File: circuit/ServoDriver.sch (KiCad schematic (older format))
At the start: 0 parts

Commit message: 変更点忘れた
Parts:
- added C?: C, symbol C
- added J?: servo0, symbol CONN_01X03
- added J? (x2): servo2, symbol CONN_01X03
- added J?: servo1, symbol CONN_01X03
- added U?: STM32F042K6Tx, LQFP32, symbol STM32F042K6Tx
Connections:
- new net +3V3: C?.1, U?.1 (VDD), U?.17 (VDDIO2), U?.5 (VDDA)
- new net GND: C?.2, U?.16 (VSS), U?.32 (VSSA)

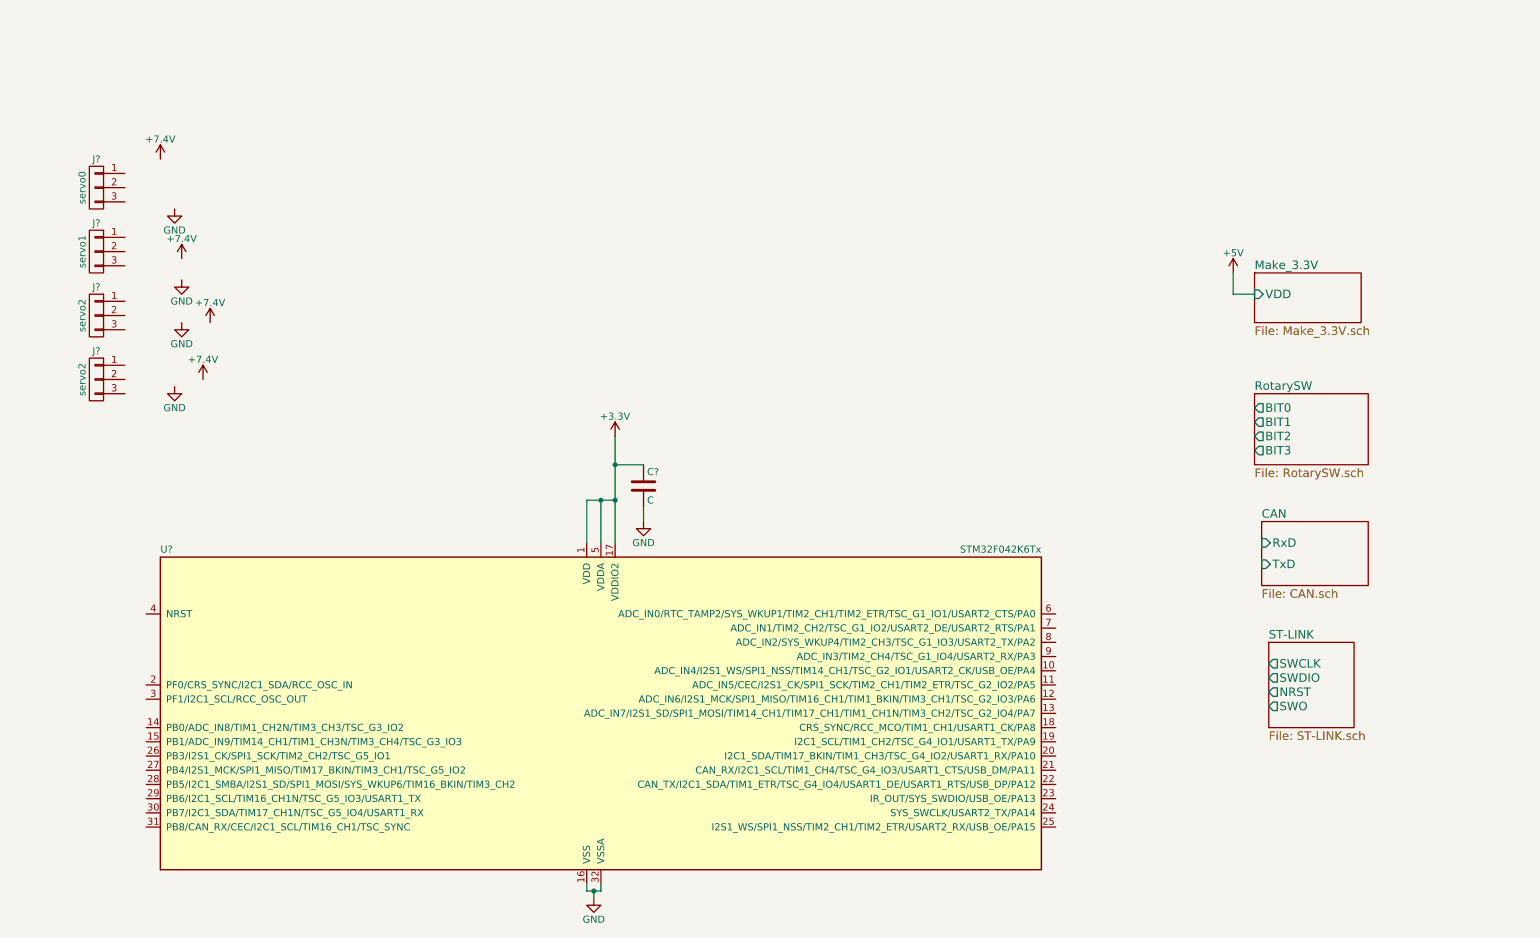
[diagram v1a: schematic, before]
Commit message: サーボの制御信号絶縁とシート分け
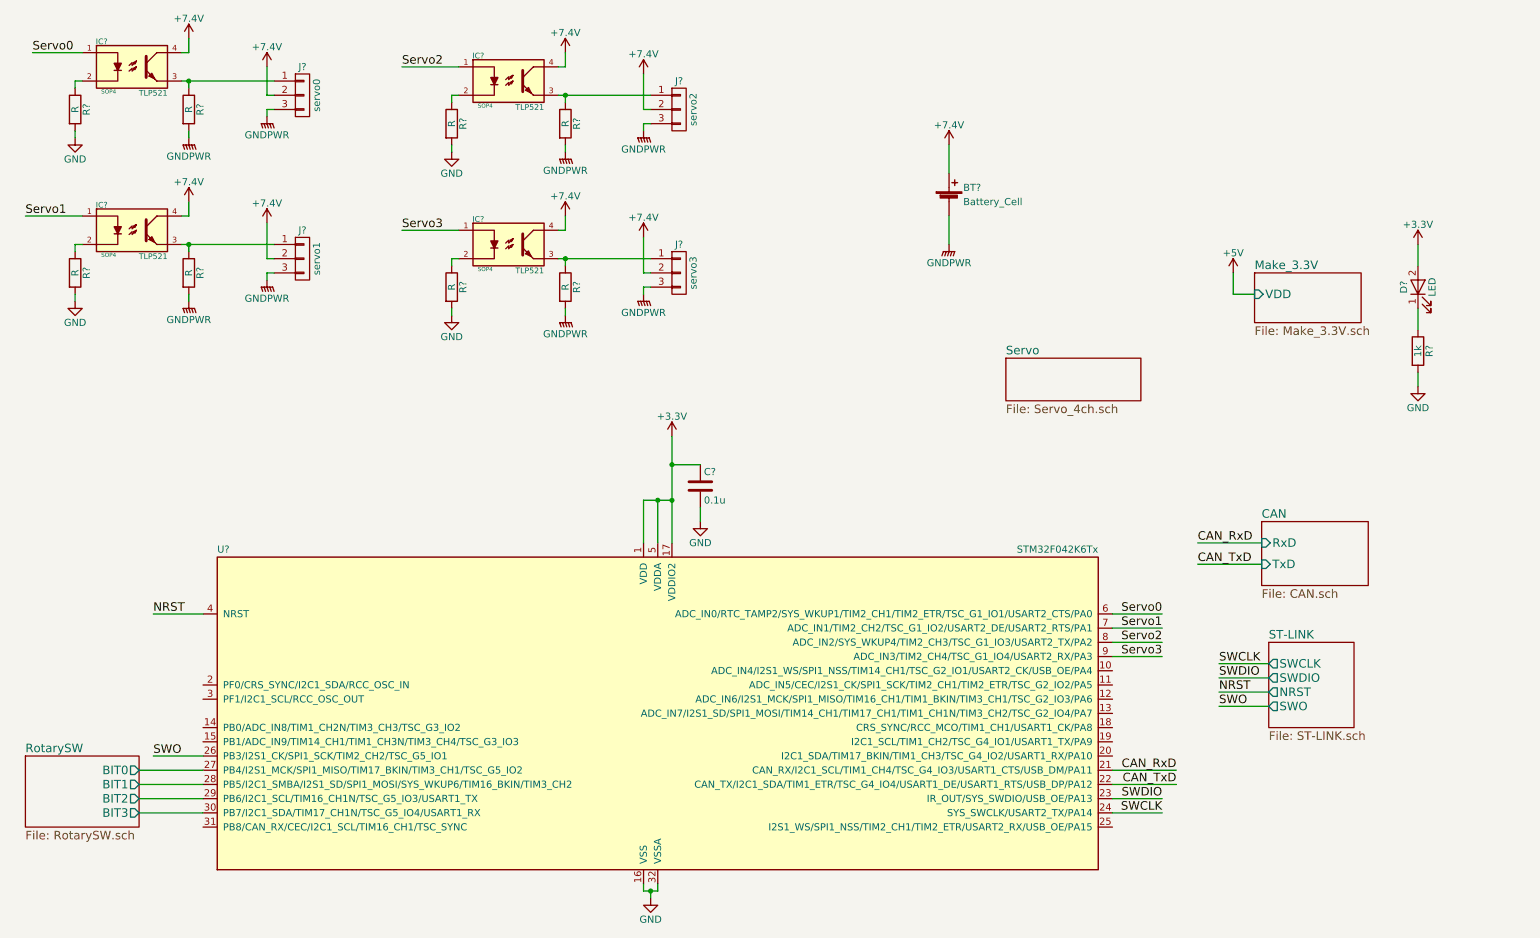
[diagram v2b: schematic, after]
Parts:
- added BT?: Battery_Cell, symbol Battery_Cell
- added D?: LED, symbol LED
- added IC? (x4): TLP521, SOP4, symbol TLP521
- added R?: 1k, symbol R
- added R? (x8): R, symbol R
- C?: value C -> 0.1u
- J?: value servo2 -> servo3
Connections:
- net +3V3: now also D?.2 (A)
- net +7.4V: now also J?.2 (P2), J?.2 (P2), J?.2 (P2), J?.2 (P2), BT?.1 (+), IC?.4, IC?.4, IC?.4, IC?.4
- net GND: now also R?.2, R?.2, R?.2, R?.2, R?.2
- net RotarySW/BIT0: now also U?.27 (PB4/I2S1_MCK/SPI1_MISO/TIM17_BKIN/TIM3_CH1/TSC_G5_IO2)
- net RotarySW/BIT1: now also U?.28 (PB5/I2C1_SMBA/I2S1_SD/SPI1_MOSI/SYS_WKUP6/TIM16_BKIN/TIM3_CH2)
- net RotarySW/BIT2: now also U?.29 (PB6/I2C1_SCL/TIM16_CH1N/TSC_G5_IO3/USART1_TX)
- net RotarySW/BIT3: now also U?.30 (PB7/I2C1_SDA/TIM17_CH1N/TSC_G5_IO4/USART1_RX)
- net CAN_RxD: now reaches U?.21 (CAN_RX/I2C1_SCL/TIM1_CH4/TSC_G4_IO3/USART1_CTS/USB_DM/PA11)
- net CAN_TxD: now reaches U?.22 (CAN_TX/I2C1_SDA/TIM1_ETR/TSC_G4_IO4/USART1_DE/USART1_RTS/USB_DP/PA12)
- net SWDIO: now reaches U?.23 (IR_OUT/SYS_SWDIO/USB_OE/PA13)
- net SWCLK: now reaches U?.24 (SYS_SWCLK/USART2_TX/PA14)
- net SWO: now reaches U?.26 (PB3/I2S1_CK/SPI1_SCK/TIM2_CH2/TSC_G5_IO1)
- net NRST: now reaches U?.4 (NRST)
- net Servo0: now reaches U?.6 (ADC_IN0/RTC_TAMP2/SYS_WKUP1/TIM2_CH1/TIM2_ETR/TSC_G1_IO1/USART2_CTS/PA0)
- net Servo0: now also IC?.1
- net Servo1: now reaches U?.7 (ADC_IN1/TIM2_CH2/TSC_G1_IO2/USART2_DE/USART2_RTS/PA1)
- net Servo1: now also IC?.1
- net Servo2: now reaches U?.8 (ADC_IN2/SYS_WKUP4/TIM2_CH3/TSC_G1_IO3/USART2_TX/PA2)
- net Servo2: now also IC?.1
- net Servo3: now reaches U?.9 (ADC_IN3/TIM2_CH4/TSC_G1_IO4/USART2_RX/PA3)
- net Servo3: now also IC?.1
- net at J?.1 (P1): now also IC?.3, R?.1 (x4)
- net GNDPWR: now reaches J?.3 (P3)
- net GNDPWR: now also J?.3 (P3), J?.3 (P3), J?.3 (P3), BT?.2 (-), R?.2, R?.2, R?.2, R?.2
- new net: D?.1 (K), R?.1
- new net: IC?.2, R?.1 (x4)
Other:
- moved on the sheet: C?, J?, U?

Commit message: 階層ピンの追加
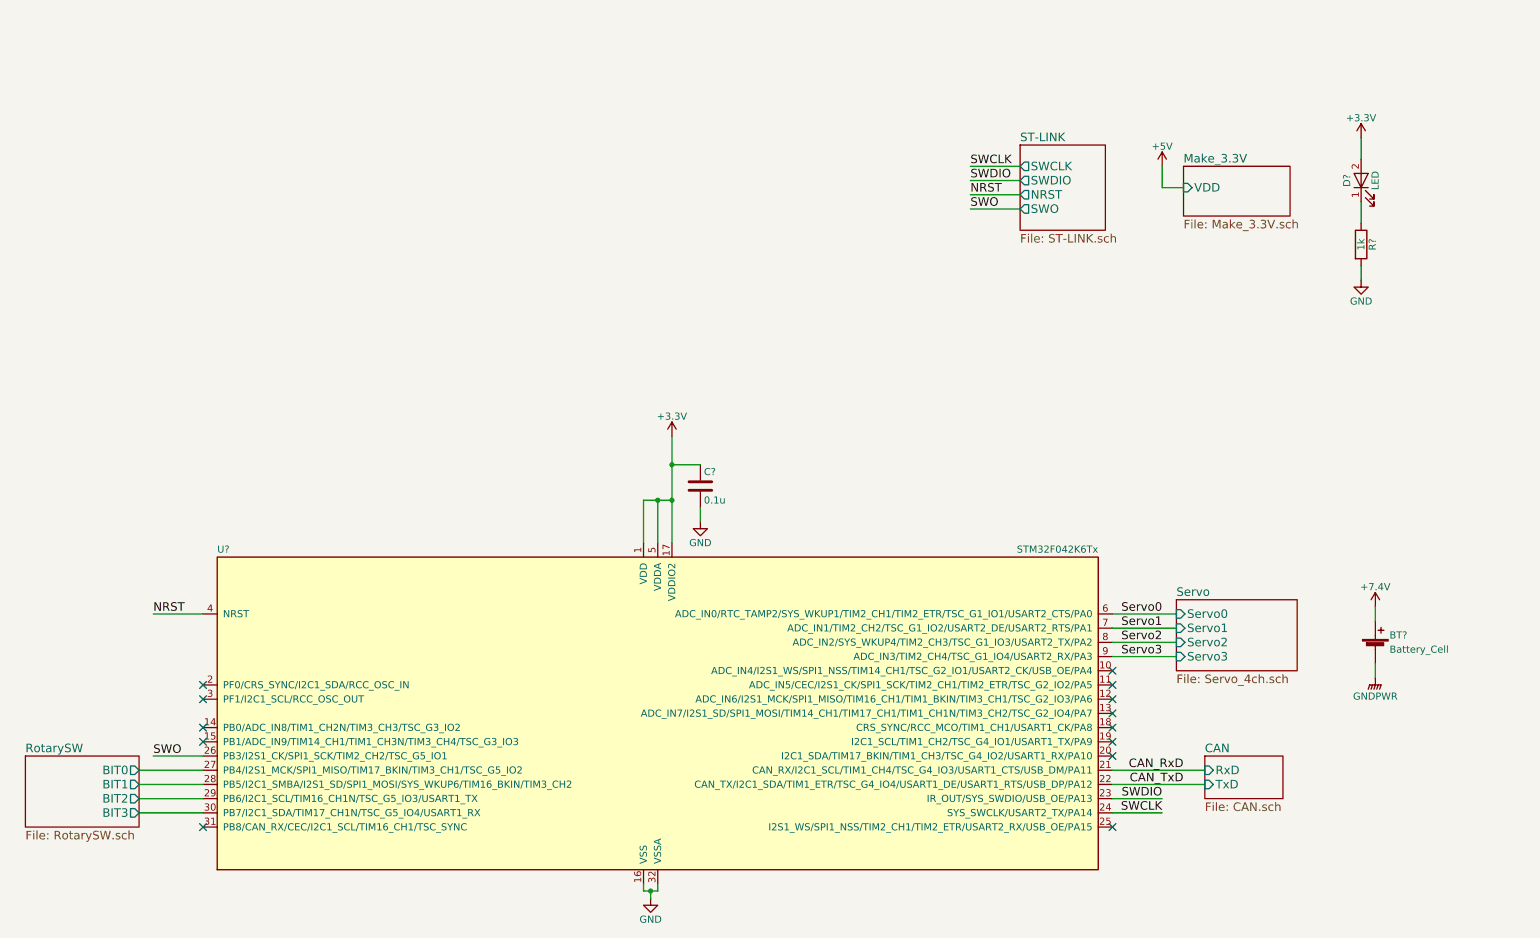
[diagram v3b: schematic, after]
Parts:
- removed IC? (x4): TLP521, SOP4, symbol TLP521
- removed J?: servo0, symbol CONN_01X03
- removed J?: servo2, symbol CONN_01X03
- removed J?: servo1, symbol CONN_01X03
- removed J?: servo3, symbol CONN_01X03
- removed R? (x8): R, symbol R
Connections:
- no-connect marks 0 -> 13
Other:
- moved on the sheet: BT?, D?, R?

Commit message: Servoのchを4->6に変更
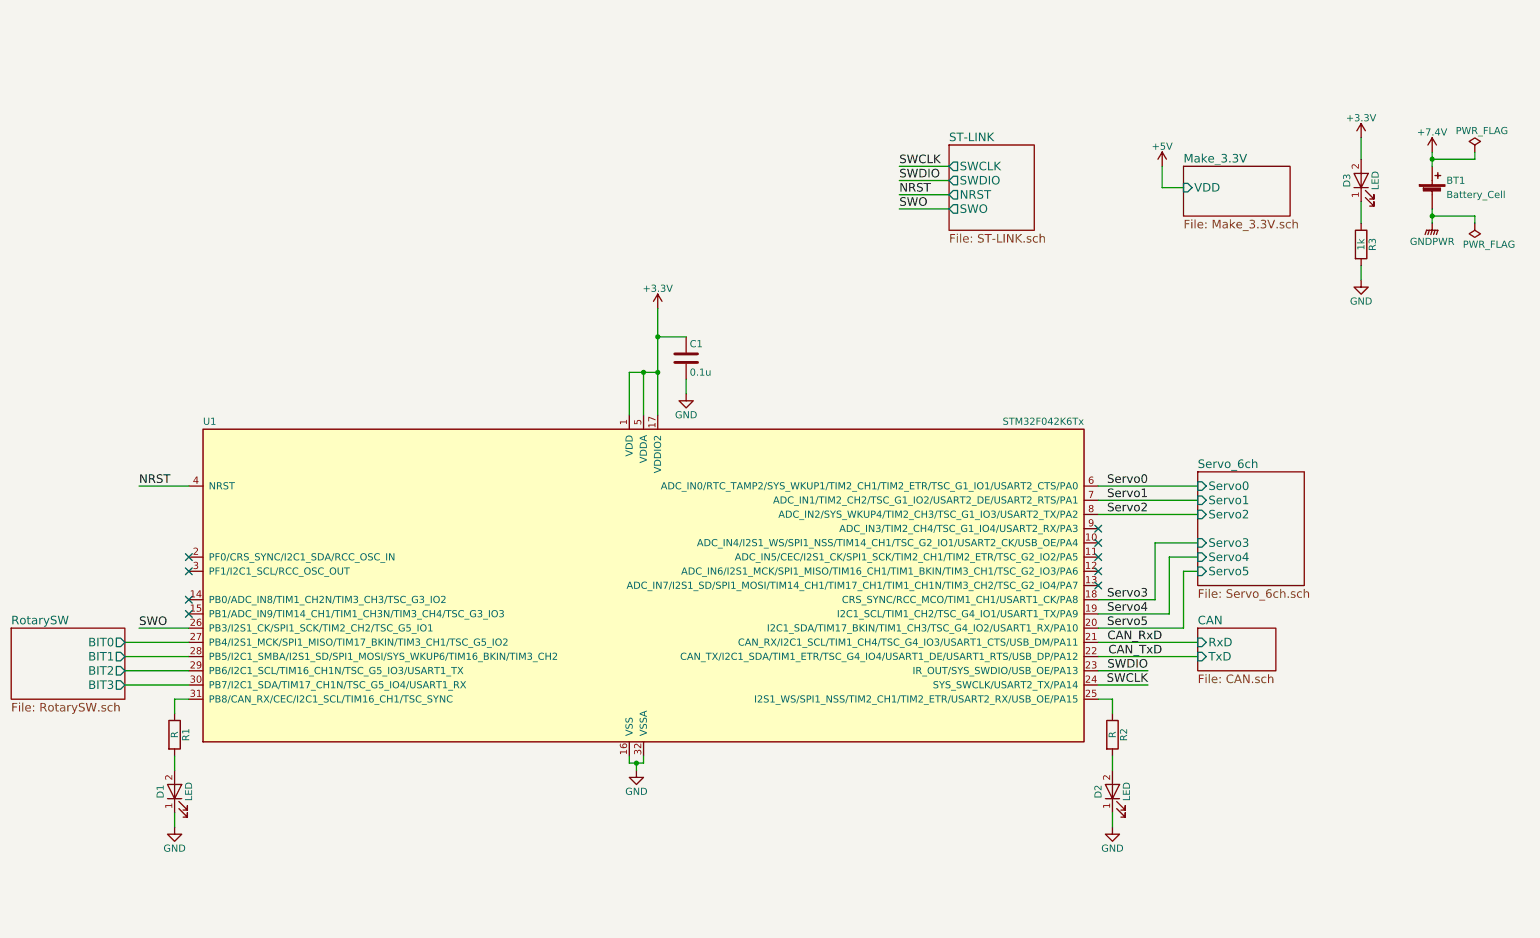
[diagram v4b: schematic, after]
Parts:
- added D1, D2: LED, LEDs:LED_D5.0mm, symbol LED
- added R1, R2: R, symbol R
- D3: renamed from D?; footprint (none) -> LEDs:LED_D5.0mm
- U1: renamed from U?; footprint LQFP32 -> Housings_QFP:TQFP-32_7x7mm_Pitch0.8mm
- gave numbers to parts that had none: 3
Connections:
- net GND: now also D1.1 (K), D2.1 (K)
- net Servo3: now also U1.18 (CRS_SYNC/RCC_MCO/TIM1_CH1/USART1_CK/PA8); no longer U1.9 (ADC_IN3/TIM2_CH4/TSC_G1_IO4/USART2_RX/PA3)
- net Servo4: now reaches U1.19 (I2C1_SCL/TIM1_CH2/TSC_G4_IO1/USART1_TX/PA9)
- net Servo5: now reaches U1.20 (I2C1_SDA/TIM17_BKIN/TIM1_CH3/TSC_G4_IO2/USART1_RX/PA10)
- net at U1.25 (I2S1_WS/SPI1_NSS/TIM2_CH1/TIM2_ETR/USART2_RX/USB_OE/PA15): now also R2.1
- net at U1.31 (PB8/CAN_RX/CEC/I2C1_SCL/TIM16_CH1/TSC_SYNC): now also R1.1
- new net: D1.2 (A), R1.2
- new net: D2.2 (A), R2.2
- no-connect marks 13 -> 9
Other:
- moved on the sheet: BT1, C1, U1

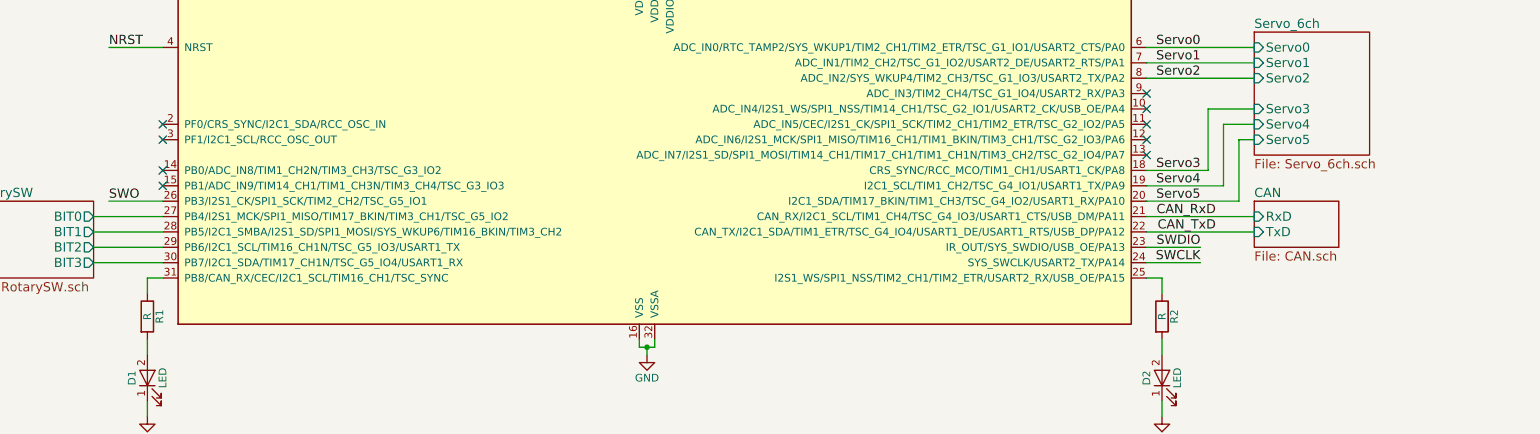
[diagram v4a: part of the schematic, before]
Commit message: 回路図と部品表完了
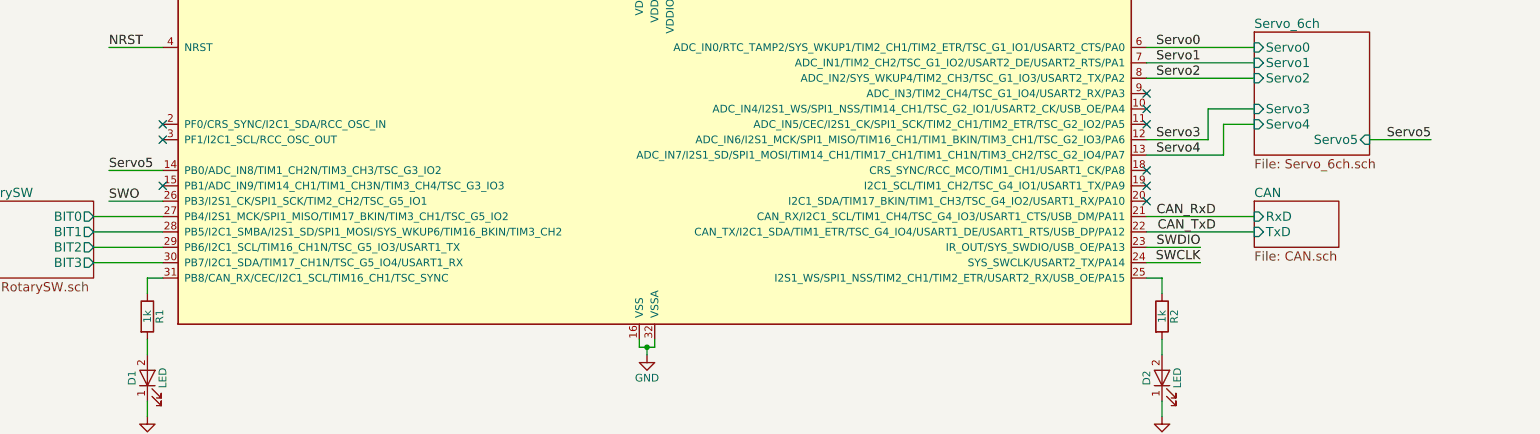
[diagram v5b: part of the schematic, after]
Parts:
- BT1: footprint (none) -> YASU:XT_M
- C1: footprint (none) -> Capacitors_SMD:C_0805_HandSoldering
- R1, R2: value R -> 1k; footprint (none) -> Resistors_SMD:R_0603_HandSoldering
- R3: footprint (none) -> Resistors_SMD:R_0603_HandSoldering
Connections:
- net Servo3: now also U1.12 (ADC_IN6/I2S1_MCK/SPI1_MISO/TIM16_CH1/TIM1_BKIN/TIM3_CH1/TSC_G2_IO3/PA6); no longer U1.18 (CRS_SYNC/RCC_MCO/TIM1_CH1/USART1_CK/PA8)
- net Servo4: now also U1.13 (ADC_IN7/I2S1_SD/SPI1_MOSI/TIM14_CH1/TIM17_CH1/TIM1_CH1N/TIM3_CH2/TSC_G2_IO4/PA7); no longer U1.19 (I2C1_SCL/TIM1_CH2/TSC_G4_IO1/USART1_TX/PA9)
- net Servo5: now also U1.14 (PB0/ADC_IN8/TIM1_CH2N/TIM3_CH3/TSC_G3_IO2); no longer U1.20 (I2C1_SDA/TIM17_BKIN/TIM1_CH3/TSC_G4_IO2/USART1_RX/PA10)
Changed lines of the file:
@@
 F 0 "C1" H 5375 2950 50  0000 L CNN
 F 1 "0.1u" H 5375 2750 50  0000 L CNN
-F 2 "" H 5388 2700 50  0001 C CNN
+F 2 "Capacitors_SMD:C_0805_HandSoldering" H 5388 2700 50  0001 C CNN
 F 3 "" H 5350 2850 50  0001 C CNN
 	1    5350 2850
@@
 F 0 "BT1" H 10700 1800 50  0000 L CNN
 F 1 "Battery_Cell" H 10700 1700 50  0000 L CNN
-F 2 "" V 10600 1760 50  0001 C CNN
+F 2 "YASU:XT_M" V 10600 1760 50  0001 C CNN
 F 3 "" V 10600 1760 50  0001 C CNN
 	1    10600 1700
@@
 F 0 "R3" V 10180 2050 50  0000 C CNN
 F 1 "1k" V 10100 2050 50  0000 C CNN
-F 2 "" V 10030 2050 50  0001 C CNN
+F 2 "Resistors_SMD:R_0603_HandSoldering" V 10030 2050 50  0001 C CNN
 F 3 "" H 10100 2050 50  0001 C CNN
 	1    10100 2050
@@
 	1    0    0    -1
 $EndComp
-Text Label 8600 4650 2    60   ~ 0
+Text Label 8600 4450 2    60   ~ 0
 Servo4
 Text Label 8600 3950 2    60   ~ 0
@@
 NoConn ~ 1850 4250
 NoConn ~ 1850 4350
-NoConn ~ 1850 4550
+NoConn ~ 8250 4550
 NoConn ~ 1850 4650
-NoConn ~ 8250 4450
-NoConn ~ 8250 4350
+NoConn ~ 8250 4750
+NoConn ~ 8250 4650
 NoConn ~ 8250 4250
 NoConn ~ 8250 4150
@@
 F5 "Servo3" I L 8950 4150 60
 F6 "Servo4" I L 8950 4250 60
-F7 "Servo5" I L 8950 4350 60
+F7 "Servo5" I R 9700 4350 60
 $EndSheet
-Text Label 8600 4550 2    60   ~ 0
+Text Label 8600 4350 2    60   ~ 0
 Servo3
-Text Label 8600 4750 2    60   ~ 0
+Text Label 10100 4350 2    60   ~ 0
 Servo5
 NoConn ~ 8250 4050
@@
 P 1750 5500
 F 0 "R1" V 1830 5500 50  0000 C CNN
-F 1 "R" V 1750 5500 50  0000 C CNN
-F 2 "" V 1680 5500 50  0001 C CNN
+F 1 "1k" V 1750 5500 50  0000 C CNN
+F 2 "Resistors_SMD:R_0603_HandSoldering" V 1680 5500 50  0001 C CNN
 F 3 "" H 1750 5500 50  0001 C CNN
 	1    1750 5500
@@
 P 8350 5500
 F 0 "R2" V 8430 5500 50  0000 C CNN
-F 1 "R" V 8350 5500 50  0000 C CNN
-F 2 "" V 8280 5500 50  0001 C CNN
+F 1 "1k" V 8350 5500 50  0000 C CNN
+F 2 "Resistors_SMD:R_0603_HandSoldering" V 8280 5500 50  0001 C CNN
 F 3 "" H 8350 5500 50  0001 C CNN
 	1    8350 5500
@@
 	10600 1400 10600 1500
 Wire Wire Line
-	8950 4350 8850 4350
-Wire Wire Line
-	8850 4350 8850 4750
-Wire Wire Line
-	8850 4750 8250 4750
-Wire Wire Line
-	8250 4650 8750 4650
-Wire Wire Line
-	8750 4650 8750 4250
-Wire Wire Line
 	8750 4250 8950 4250
-Wire Wire Line
-	8650 4550 8250 4550
-Wire Wire Line
-	8650 4550 8650 4150
 Wire Wire Line
 	8650 4150 8950 4150
@@
 	-1   0    0    1
 $EndComp
+Wire Wire Line
+	8650 4150 8650 4350
+Wire Wire Line
+	8650 4350 8250 4350
+Wire Wire Line
+	8250 4450 8750 4450
+Wire Wire Line
+	8750 4450 8750 4250
+Wire Wire Line
+	9700 4350 10100 4350
+Text Label 1500 4550 0    60   ~ 0
+Servo5
+Wire Wire Line
+	1500 4550 1850 4550
 $EndSCHEMATC
